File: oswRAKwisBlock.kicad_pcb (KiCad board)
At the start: 4 copper layers, 33.8 x 46 mm, 70 parts, among them J1 WisBlock, J2 0524352471, J4 10114830-10102LF, J5 USB micro, Q1 SI1308EDL-T1-GE3, U1 MCP73811T-420I/OT, U2 MAX2769B, U3 MAX8510EXK29+T, U4 MAX8510EXK29+T, U5 MIC5365-3.0YC5-TR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

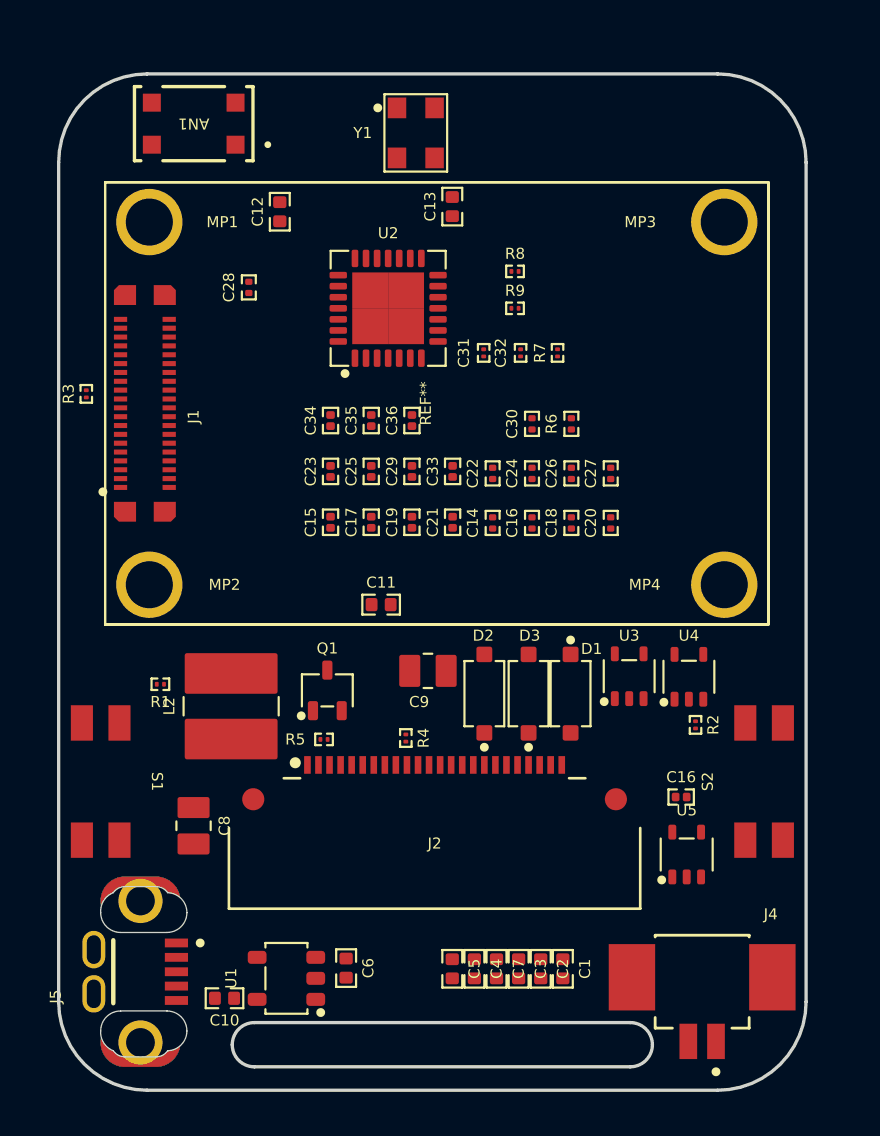
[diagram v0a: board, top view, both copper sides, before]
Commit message: Moving parts around to start layout.
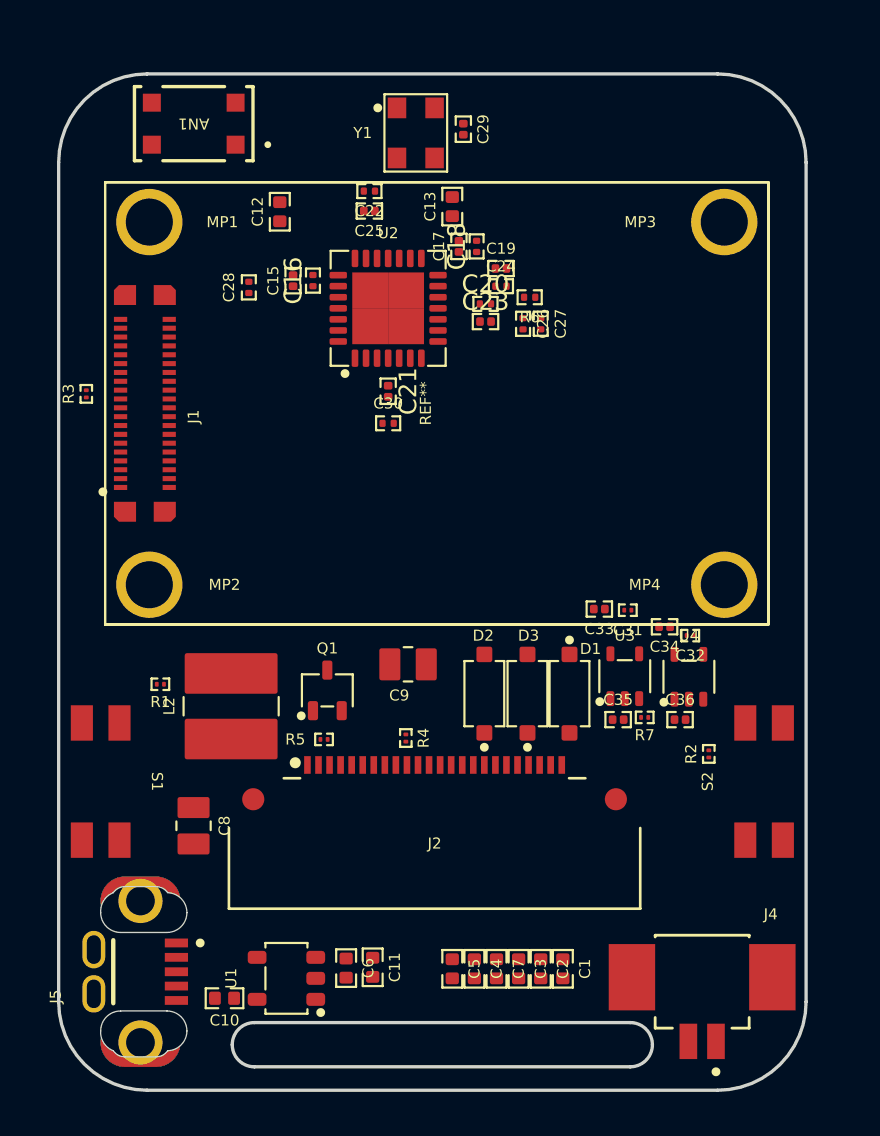
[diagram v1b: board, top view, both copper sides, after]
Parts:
- removed C14: 100p, AllardChip:CAPC60X30X33L15L
- removed the C16 at (141.3, 120.3)
- removed the C16 at (148.0, 132.7)
- removed R8, R9: 10k, AllardChip:RESC40X20X15L10L
- removed the REF** at (136.8, 122.5)
- removed U5: MIC5365-3.0YC5-TR, AllardSOT:SOT23-5P65_210X110L33X22L
- added C16: 100p, AllardChip:CAPC60X30X33L15L, F.Cu at (131.3, 109.3)
- moved C36 18.2 mm to (147.9, 129.2), turned to 0 degrees
- moved C34 17.8 mm to (147.2, 125.0), turned to 180 degrees
- moved C35 17.5 mm to (145.2, 129.2), turned to 0 degrees
- moved R7 16.9 mm to (146.3, 129.1), turned to 180 degrees
- moved C11 16.4 mm to (134.1, 140.4), turned to -90 degrees
- moved C29 15.6 mm to (138.2, 102.5), turned to -90 degrees
- moved C32 14.9 mm to (148.4, 125.4), turned to 180 degrees
- moved C22 13.9 mm to (133.9, 105.3), turned to 180 degrees
- moved C31 13.3 mm to (145.6, 124.2), turned to 180 degrees
- moved C18 13.2 mm to (138.8, 107.8)
- moved C17 13.1 mm to (137.9, 107.8)
- moved C19 12.2 mm to (139.9, 108.8), turned to 0 degrees
- moved C25 11.8 mm to (133.9, 106.2), turned to 180 degrees
- moved C20 11.4 mm to (139.2, 110.4), turned to 0 degrees
- moved C15 11.1 mm to (130.4, 109.3)
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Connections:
- J1 pad 22: /~{GPS_PWR_SHDN} -> unconnected-(J1-AIN1-Pad22)
- J1 pad 23: Net-(J1-BOOT) -> unconnected-(J1-BOOT-Pad23)
- J1 pad 24: /~{GPS_SHDN} -> unconnected-(J1-IO7-Pad24)
- J1 pad 25: /SS -> unconnected-(J1-SPI_CS-Pad25)
- J1 pad 26: /SCLK -> unconnected-(J1-SPI_CLK-Pad26)
- J1 pad 27: /GPS_MISO -> unconnected-(J1-SPI_MISO-Pad27)
- J1 pad 28: /MOSI -> unconnected-(J1-SPI_MOSI-Pad28)
- J1 pad 29: /BUSY -> unconnected-(J1-IO1-Pad29)
- J1 pad 30: /BTN1 -> unconnected-(J1-IO2-Pad30)
- J1 pad 31: /RES -> unconnected-(J1-IO3-Pad31)
- J1 pad 32: /BTN2 -> unconnected-(J1-IO4-Pad32)
- J1 pad 37: /~{GPS_IDLE} -> unconnected-(J1-IO5-Pad37)
- J1 pad 38: /~{GPS_CS} -> unconnected-(J1-IO6-Pad38)
- R7 pad 2: /~{GPS_PWR_SHDN} -> /gpsMod/~{GPS_PWR_SHDN}
- U2 pad 10: /~{GPS_CS} -> /gpsMod/~{GPS_CS}
- U2 pad 24: /~{GPS_IDLE} -> /gpsMod/~{GPS_IDLE}
- U2 pad 7: /~{GPS_SHDN} -> /gpsMod/~{GPS_SHDN}
- U2 pad 8: /GPS_MISO -> /gpsMod/GPS_MISO
- U2 pad 9: /SCLK -> /gpsMod/GPS_SCLK
- U3 pad 3: /~{GPS_PWR_SHDN} -> /gpsMod/~{GPS_PWR_SHDN}
- U4 pad 3: /~{GPS_PWR_SHDN} -> /gpsMod/~{GPS_PWR_SHDN}

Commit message: starting to lay the board out.
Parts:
- added C16: 1uF, AllardChip:CAPC60X30X39L17L, F.Cu at (147.0, 130.6)
- added R8: 10k, AllardChip:RESC40X20X15L10L, F.Cu at (121.2, 114.3)
- added R9: 10k, AllardChip:RESC40X20X15L10L, F.Cu at (127.1, 114.7)
- added U5: MIC5365-3.0YC5-TR, AllardSOT:SOT23-5P65_210X110L33X22L, F.Cu at (148.2, 133.1)
- moved C13 16.6 mm to (126.4, 118.2), turned to -90 degrees
- moved C12 15.0 mm to (121.0, 118.3), turned to -90 degrees
- moved R3 1.84 mm to (121.2, 116.3), turned to 0 degrees
- moved R1 1.75 mm to (124.3, 129.3)
- moved C3 1.00 mm to (139.7, 140.5)
- moved C7 0.95 mm to (140.6, 140.5)
- moved C34 0.70 mm to (147.2, 124.3)
- moved C22 0.10 mm to (133.9, 105.4)
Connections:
- J1 pad 22: unconnected-(J1-AIN1-Pad22) -> /~{GPS_PWR_SHDN}
- J1 pad 23: unconnected-(J1-BOOT-Pad23) -> Net-(J1-BOOT)
- J1 pad 24: unconnected-(J1-IO7-Pad24) -> /~{GPS_SHDN}
- J1 pad 25: unconnected-(J1-SPI_CS-Pad25) -> /SS
- J1 pad 26: unconnected-(J1-SPI_CLK-Pad26) -> /SCLK
- J1 pad 27: unconnected-(J1-SPI_MISO-Pad27) -> /GPS_MISO
- J1 pad 28: unconnected-(J1-SPI_MOSI-Pad28) -> /MOSI
- J1 pad 29: unconnected-(J1-IO1-Pad29) -> /BUSY
- J1 pad 30: unconnected-(J1-IO2-Pad30) -> /BTN1
- J1 pad 31: unconnected-(J1-IO3-Pad31) -> /RES
- J1 pad 32: unconnected-(J1-IO4-Pad32) -> /BTN2
- J1 pad 37: unconnected-(J1-IO5-Pad37) -> /~{GPS_IDLE}
- J1 pad 38: unconnected-(J1-IO6-Pad38) -> /~{GPS_CS}
- J1 pad FS3: (no net) -> GND
- R7 pad 2: /gpsMod/~{GPS_PWR_SHDN} -> /~{GPS_PWR_SHDN}
- U2 pad 10: /gpsMod/~{GPS_CS} -> /~{GPS_CS}
- U2 pad 24: /gpsMod/~{GPS_IDLE} -> /~{GPS_IDLE}
- U2 pad 7: /gpsMod/~{GPS_SHDN} -> /~{GPS_SHDN}
- U2 pad 8: /gpsMod/GPS_MISO -> /GPS_MISO
- U2 pad 9: /gpsMod/GPS_SCLK -> /SCLK
- U3 pad 3: /gpsMod/~{GPS_PWR_SHDN} -> /~{GPS_PWR_SHDN}
- U4 pad 3: /gpsMod/~{GPS_PWR_SHDN} -> /~{GPS_PWR_SHDN}
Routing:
- net GND: track 0.00 -> 58.0 mm, vias 0 -> 32
- net Net-(U1-V_{BAT}): track 0.00 -> 31.0 mm, vias 0 -> 2
- net VDD: track 0.00 -> 28.9 mm
- net Net-(Q1-D): track 0.00 -> 15.9 mm
- net VDD_GPS_A: track 0.00 -> 12.5 mm
- net /PREVGH: track 0.00 -> 10.5 mm
- net VDD_GPS_B: track 0.00 -> 9.71 mm
- net Net-(J2-Pin_20): track 0.00 -> 9.18 mm
- net Net-(J2-Pin_18): track 0.00 -> 9.18 mm
- net Net-(D1-K): track 0.00 -> 8.92 mm
- net Net-(J2-Pin_5): track 0.00 -> 8.86 mm, vias 0 -> 2
- net Net-(J2-Pin_24): track 0.00 -> 8.81 mm
- net Net-(J2-Pin_22): track 0.00 -> 8.81 mm
- net /BTN2: track 0.00 -> 7.69 mm
- net /BTN1: track 0.00 -> 6.89 mm
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- added copper zone on In1.Cu, net GND

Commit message: Moving some stuff around.
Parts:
- moved J5 0.11 mm to (123.5, 140.5)
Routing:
- net GND: track 58.0 -> 0.00 mm, vias 32 -> 0
- net Net-(U1-V_{BAT}): track 31.0 -> 0.00 mm, vias 2 -> 0
- net VDD: track 28.9 -> 0.00 mm
- net Net-(Q1-D): track 15.9 -> 0.00 mm
- net VDD_GPS_A: track 12.5 -> 0.00 mm
- net /PREVGH: track 10.5 -> 0.00 mm
- net VDD_GPS_B: track 9.71 -> 0.00 mm
- net Net-(J2-Pin_20): track 9.18 -> 0.00 mm
- net Net-(J2-Pin_18): track 9.18 -> 0.00 mm
- net Net-(D1-K): track 8.92 -> 0.00 mm
- net Net-(J2-Pin_5): track 8.86 -> 0.00 mm, vias 2 -> 0
- net Net-(J2-Pin_24): track 8.81 -> 0.00 mm
- net Net-(J2-Pin_22): track 8.81 -> 0.00 mm
- net /BTN2: track 7.69 -> 0.00 mm
- net /BTN1: track 6.89 -> 0.00 mm
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
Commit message: Moving some stuff around.
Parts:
- removed R9: 10k, AllardChip:RESC40X20X15L10L
- moved J4 37.8 mm to (124.5, 112.2), turned to 0 degrees
- moved U5 29.6 mm to (122.8, 117.9)
- moved MP1 25.4 mm to (149.0, 102.5), turned to -90 degrees
- moved C36 25.1 mm to (126.3, 116.4), turned to -90 degrees
- moved C12 22.8 mm to (139.8, 105.5), turned to 0 degrees
- moved U4 22.7 mm to (128.2, 116.7), turned to -90 degrees
- moved MP2 22.3 mm to (132.6, 102.5), turned to -90 degrees
- moved MP3 21.8 mm to (149.0, 128.5), turned to -90 degrees
- moved C35 21.4 mm to (126.3, 118.9), turned to -90 degrees
- moved J1 21.2 mm to (140.8, 102.3), turned to 0 degrees
- moved R7 21.0 mm to (127.2, 120.7), turned to 90 degrees
- moved C32 20.1 mm to (130.1, 117.1), turned to 90 degrees
- moved C11 20.1 mm to (128.4, 121.1), turned to 0 degrees
- moved C34 19.1 mm to (130.2, 115.8), turned to 90 degrees
- moved U3 19.0 mm to (128.2, 119.2), turned to -90 degrees
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
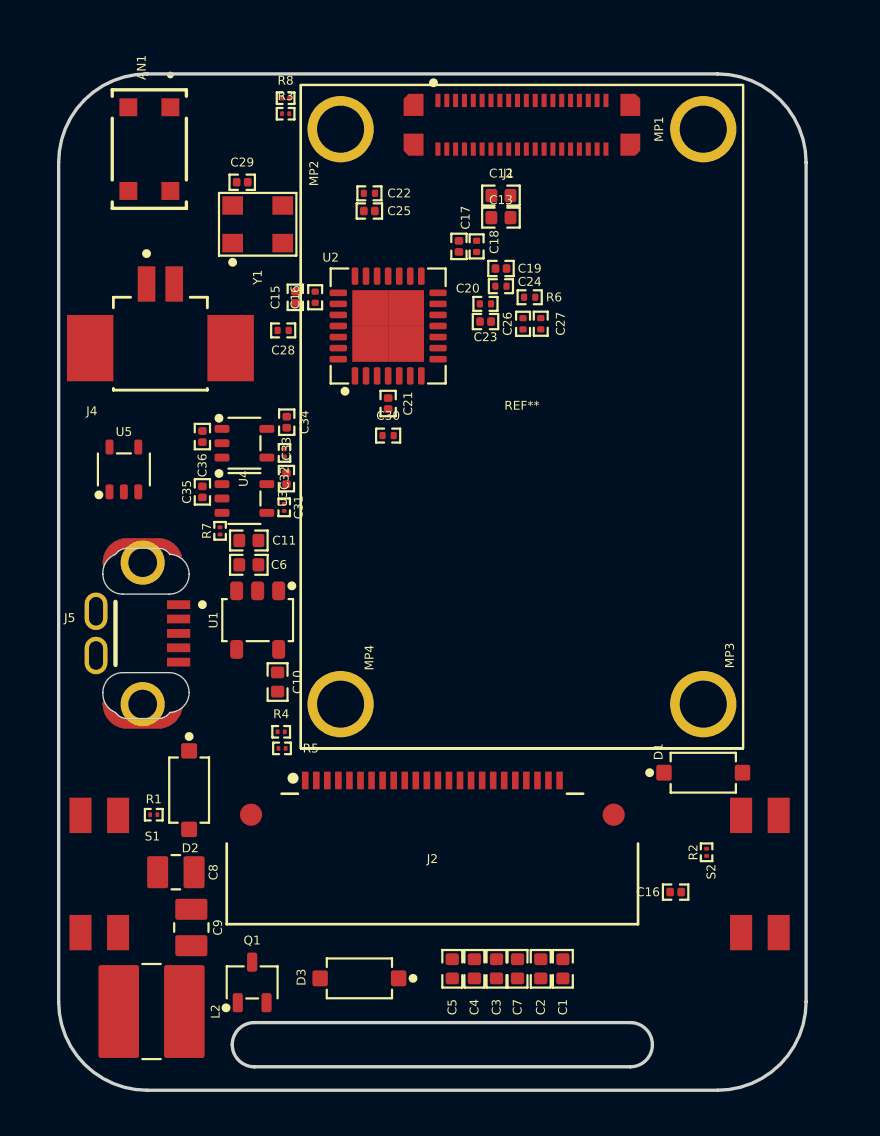
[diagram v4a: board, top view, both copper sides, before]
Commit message: Mirroring layout to match watchy layout better.
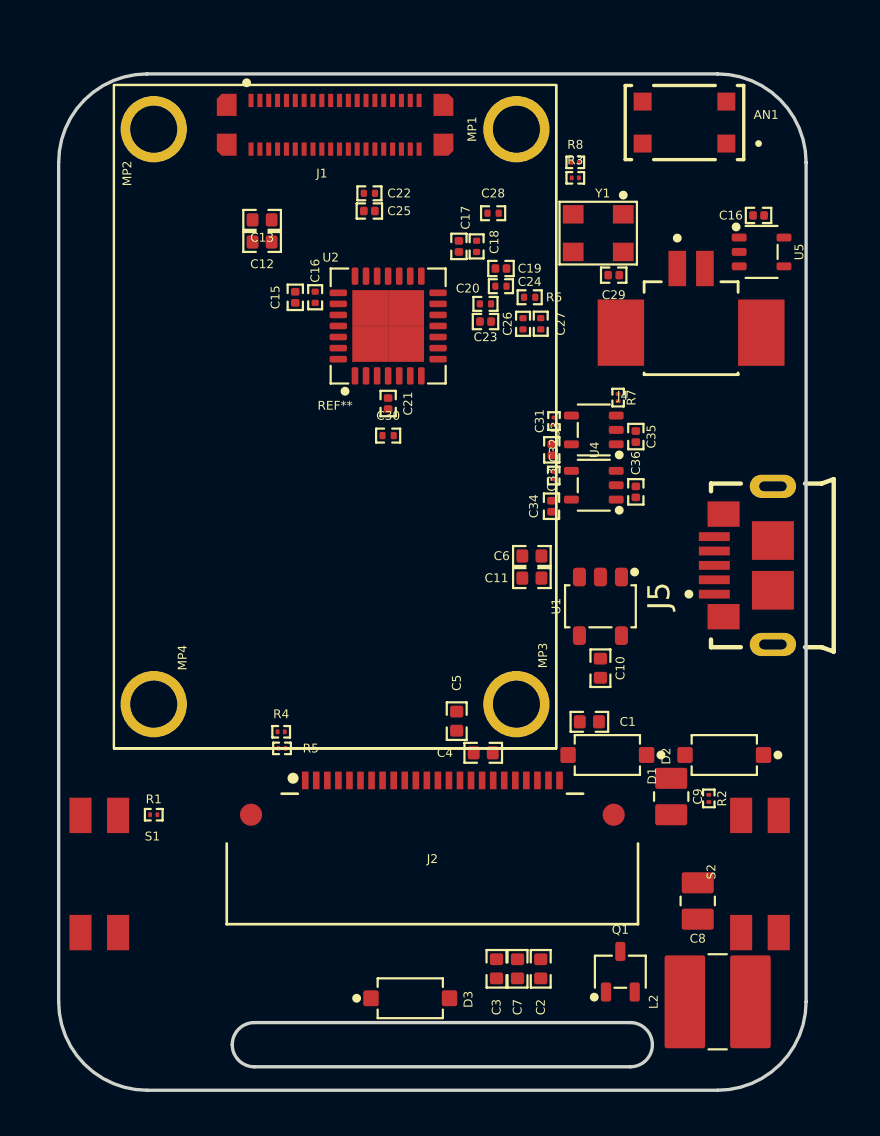
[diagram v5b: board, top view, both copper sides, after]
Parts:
- J5: footprint AllardConnFootPrints:GCT_USB3190-GF-C -> AllardFootPrints:GCT_USB3075-30-A
- moved C16 30.8 mm to (151.5, 106.4)
- moved U5 30.5 mm to (151.6, 108.0), turned to -90 degrees
- moved J5 25.9 mm to (149.5, 123.5)
- moved L2 25.6 mm to (149.7, 142.0), turned to 180 degrees
- moved D2 24.3 mm to (149.9, 130.8), turned to 180 degrees
- moved AN1 24.2 mm to (148.2, 102.2), turned to 180 degrees
- moved J4 24.0 mm to (148.4, 111.5)
- moved C8 23.6 mm to (148.8, 137.4), turned to 90 degrees
- moved C9 22.5 mm to (147.6, 132.7)
- moved C35 19.8 mm to (145.9, 116.4), turned to 90 degrees
- moved C36 19.8 mm to (145.9, 118.9), turned to 90 degrees
- moved R7 19.0 mm to (145.2, 114.6), turned to -90 degrees
- moved C29 17.3 mm to (144.9, 109.1), turned to 180 degrees
- moved Q1 16.7 mm to (145.2, 140.6)
- moved U3 16.1 mm to (144.1, 116.1), turned to 90 degrees
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
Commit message: Adding mounting holes.
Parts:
- added H1: MountingHole, MountingHole:MountingHole_2.2mm_M2, F.Cu at (149.8, 103.0)
- added H2: MountingHole, MountingHole:MountingHole_2.2mm_M2, F.Cu at (123.8, 142.0)
- moved R3 6.05 mm to (137.3, 105.8)
- moved R8 6.05 mm to (137.3, 105.1)
- moved AN1 3.60 mm to (144.7, 103.0), turned to -90 degrees
- moved C29 0.20 mm to (144.9, 109.3)
- moved Y1 0.20 mm to (144.2, 107.4)

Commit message: working on the layout some.
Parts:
- moved C6 12.3 mm to (132.5, 130.4)
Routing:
- net GND: track 0.00 -> 37.3 mm, vias 0 -> 21
- net /PREVGH: track 0.00 -> 17.8 mm, vias 0 -> 2
- net Net-(Q1-D): track 0.00 -> 14.4 mm
- net VDD_GPS_A: track 0.00 -> 11.0 mm
- net VDD_GPS_B: track 0.00 -> 10.2 mm
- net VUSB_BUS: track 0.00 -> 9.80 mm
- net VDD: track 0.00 -> 8.89 mm
- net Net-(J2-Pin_20): track 0.00 -> 8.44 mm
- net Net-(J2-Pin_22): track 0.00 -> 8.15 mm
- net /RES: track 0.00 -> 7.06 mm
- net /BTN2: track 0.00 -> 7.01 mm
- net /BTN1: track 0.00 -> 6.76 mm
- net Net-(J2-Pin_24): track 0.00 -> 4.24 mm
- net Net-(U2-LNAOUT): track 0.00 -> 3.01 mm
- net Net-(U2-MIXIN): track 0.00 -> 2.80 mm
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
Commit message: Working on connect the dots.....
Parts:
- moved C27 13.3 mm to (128.3, 111.6), turned to 90 degrees
- moved R6 12.6 mm to (128.8, 112.8), turned to 0 degrees
- moved C26 11.7 mm to (129.2, 111.6), turned to 90 degrees
- moved C19 11.1 mm to (130.1, 114.1), turned to 180 degrees
- moved C22 11.0 mm to (135.9, 116.2), turned to 0 degrees
- moved C18 10.5 mm to (131.2, 115.1), turned to -90 degrees
- moved C24 10.4 mm to (130.2, 113.3), turned to 180 degrees
- moved C30 9.84 mm to (135.2, 106.5), turned to 180 degrees
- moved C25 9.43 mm to (135.9, 115.4), turned to 0 degrees
- moved C17 9.38 mm to (132.1, 115.1), turned to -90 degrees
- moved C15 9.30 mm to (139.4, 112.8), turned to -90 degrees
- moved C20 8.56 mm to (130.8, 112.5), turned to 180 degrees
- moved C23 8.31 mm to (130.8, 111.5), turned to 180 degrees
- moved C16 7.59 mm to (138.6, 112.8), turned to -90 degrees
- moved C21 6.94 mm to (135.2, 108.0), turned to 90 degrees
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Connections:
- J1 pad 9: unconnected-(J1-VBUS-Pad9) -> VUSB_BUS
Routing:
- net GND: track 37.3 -> 70.4 mm, vias 21 -> 74
- net /USB_-: track 0.00 -> 30.6 mm, vias 0 -> 2
- net /USB_+: track 0.00 -> 30.2 mm, vias 0 -> 2
- net /~{GPS_PWR_SHDN}: track 0.69 -> 28.0 mm, vias 0 -> 2
- net /GDR: track 2.31 -> 24.2 mm, vias 0 -> 2
- net /~{MCU_RES}: track 0.00 -> 14.5 mm
- net Net-(U2-XTAL): track 0.00 -> 13.6 mm, vias 0 -> 2
- net unconnected-(J5-Shield-Pad6): track 0.00 -> 12.6 mm
- net /~{GPS_CS}: track 0.00 -> 12.4 mm, vias 0 -> 2
- net /GPS_MISO: track 0.00 -> 12.2 mm, vias 0 -> 4
- net VDD: track 8.89 -> 21.0 mm
- net Net-(AN1-FD): track 0.00 -> 11.6 mm
- net Net-(J1-BOOT): track 0.00 -> 10.6 mm
- net VDD_GPS_B: track 10.2 -> 20.6 mm
- net Net-(Q1-D): track 14.4 -> 23.1 mm
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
